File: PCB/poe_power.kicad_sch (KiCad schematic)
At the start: 44 parts, among them J1 Barrel_Jack, J7 Conn_01x02, Q1 MMBF170, U2 AP62200, U3 TPS2372, U6 MCP1792x-5002xCB, U7 VCB4805SBO-50WR3

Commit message: Started on board layout
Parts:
- removed J7: Conn_01x02, TerminalBlock_Phoenix:TerminalBlock_Phoenix_MKDS-1,5-2-5.08_1x02_P5.08mm_Horizontal, symbol Connector_Generic:Conn_01x02
- added J4: Screw_Terminal_01x02, TerminalBlock_Phoenix:TerminalBlock_Phoenix_MKDS-1,5-2-5.08_1x02_P5.08mm_Horizontal, symbol Connector:Screw_Terminal_01x02
- C19, C21: footprint (none) -> Capacitor_SMD:C_0805_2012Metric
- C20: footprint (none) -> Capacitor_SMD:C_Elec_6.3x5.8
- C23, C24, C25: footprint (none) -> Capacitor_SMD:C_Elec_6.3x5.4
- C6, C8: footprint Capacitor_SMD:C_0805_2012Metric_Pad1.18x1.45mm_HandSolder -> Capacitor_SMD:C_0805_2012Metric
- F1: footprint (none) -> Fuse:Fuse_1206_3216Metric
- L3: footprint (none) -> Inductor_SMD:L_0805_2012Metric
- R15, R16, R17, R18, R19, R20, R21, R22, R24, R25, R26, R29: footprint (none) -> Resistor_SMD:R_0805_2012Metric
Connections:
- net GND: now also J4.1 (Pin_1)
- net VIN: now also J4.2 (Pin_2)

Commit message: Started serious board layout
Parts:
- removed U2: AP62200, Package_TO_SOT_SMD:SOT-563, symbol Regulator_Switching:AP62250Z6
- added U2: AP62200WU-7, Package_TO_SOT_SMD:TSOT-23-6, symbol ProjectLibrary:AP62200WU-7
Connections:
- net GND: now also U2.1 (GND)
- net VIN: now also C7.1, C8.1
- net at R1.2, R4.1: now also U2.4 (FB)
- net at C1.1: now also U2.6 (BST)
- net at C1.2, L1.1: now also U2.2 (SW)
- net VLED: no longer names the net of C3.1, C4.1, L3.2
- net VLED: now also U2.3 (VIN), U2.5 (EN); no longer C7.1, C8.1

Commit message: Almost-Almost PCB design. Minor improvements on copper layer Silkscreen cleanup schematic sheet cleanup (now with subsheet titles)
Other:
- title: (none) -> Addressable LED Controller
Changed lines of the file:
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@@
 (kicad_sch (version 20230121) (generator eeschema)
   (paper "A4")
+  (title_block
+    (title "Addressable LED Controller")
+    (date "2023-07-30")
+    (rev "3.0")
+    (comment 1 "Jamal Bouajjaj")
+    (comment 2 "POE")
+  )
   (junction (at 138.43 146.05) (diameter 0) (color 0 0 0 0)
   )

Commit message: Final Rev 3 board
Many changes that are finalization changes mostly
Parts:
- removed Q1: MMBF170, Package_TO_SOT_SMD:SOT-23, symbol Transistor_FET:MMBF170
- added JP2: Jumper_2_Bridged, Connector_PinHeader_2.54mm:PinHeader_1x02_P2.54mm_Vertical, symbol Jumper:Jumper_2_Bridged
- U3: footprint Package_DFN_QFN:Texas_S-PVQFN-N20_EP3.15x3.15mm -> ProjectFootprints:TI_RGW0020B
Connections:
- net at R15.2, R22.1: now also JP2.2 (B)
- net at C19.2, D2.2 (-), D3.2 (-)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: now also JP2.1 (A)
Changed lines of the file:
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@@
-    (stroke (width 0) (type default))
-  )
-  (wire (pts (xy 106.68 53.34) (xy 106.68 50.8))
     (stroke (width 0) (type default))
   )
@@
     (stroke (width 0) (type default))
   )
-  (wire (pts (xy 88.9 77.47) (xy 113.03 77.47))
-    (stroke (width 0) (type default))
-  )
   (wire (pts (xy 106.68 146.05) (xy 111.76 146.05))
     (stroke (width 0) (type default))
@@
     (stroke (width 0) (type default))
   )
+  (wire (pts (xy 88.9 77.47) (xy 113.03 77.47))
+    (stroke (width 0) (type default))
+  )
   (wire (pts (xy 233.68 60.96) (xy 233.68 63.5))
+    (stroke (width 0) (type default))
+  )
+  (wire (pts (xy 106.68 50.8) (xy 106.68 53.34))
     (stroke (width 0) (type default))
   )
@@
     (effects (font (size 1.27 1.27)) (justify right))
   )
-  (hierarchical_label "POE_DIS" (shape input) (at 99.06 58.42 180) (fields_autoplaced)
-    (effects (font (size 1.27 1.27)) (justify right))
-  )
   (hierarchical_label "ETH_V2-" (shape input) (at 40.64 67.31 180) (fields_autoplaced)
     (effects (font (size 1.27 1.27)) (justify right))
@@
   (hierarchical_label "ETH_V1+" (shape input) (at 40.64 26.67 180) (fields_autoplaced)
     (effects (font (size 1.27 1.27)) (justify right))
+  )
+  (netclass_flag "" (length 2.54) (shape round) (at 82.55 43.18 0) (fields_autoplaced)
+    (effects (font (size 1.27 1.27)) (justify left bottom))
+    (property "Netclass" "HI_V" (at 83.439 40.64 0)
+      (effects (font (size 1.27 1.27) italic) (justify left))
+    )
+  )
+  (netclass_flag "" (length 2.54) (shape round) (at 73.66 50.8 0) (fields_autoplaced)
+    (effects (font (size 1.27 1.27)) (justify left bottom))
+    (property "Netclass" "HI_V" (at 74.549 48.26 0)
+      (effects (font (size 1.27 1.27) italic) (justify left))
+    )
   )
   (symbol (lib_id "Device:R") (at 121.92 48.26 90) (unit 1)
@@
         (path "/c2ef8e0f-ce81-4c82-a0ca-f054c5c3745d/1b44e26a-d4f8-4fcd-b6ed-54ad79d16191"
           (reference "D1") (unit 1)
-        )
-      )
-    )
-  )
-  (symbol (lib_id "Transistor_FET:MMBF170") (at 104.14 58.42 0) (unit 1)
-    (in_bom yes) (on_board yes) (dnp no)
-    (property "Reference" "Q1" (at 106.68 54.61 0)
-      (effects (font (size 1.27 1.27)) (justify left))
-    )
-    (property "Value" "MMBF170" (at 95.25 54.61 0)
-      (effects (font (size 1.27 1.27)) (justify left))
-    )
-    (property "Footprint" "Package_TO_SOT_SMD:SOT-23" (at 109.22 60.325 0)
-      (effects (font (size 1.27 1.27) italic) (justify left) hide)
-    )
-    (property "Datasheet" "https://www.diodes.com/assets/Datasheets/ds30104.pdf" (at 104.14 58.42 0)
-      (effects (font (size 1.27 1.27)) (justify left) hide)
-    )
-    (pin "1")
-    (pin "2")
-    (pin "3")
-    (instances
-      (project "LED_Controller"
-        (path "/c2ef8e0f-ce81-4c82-a0ca-f054c5c3745d"
-          (reference "Q1") (unit 1)
-        )
-        (path "/c2ef8e0f-ce81-4c82-a0ca-f054c5c3745d/1b44e26a-d4f8-4fcd-b6ed-54ad79d16191"
-          (reference "Q1") (unit 1)
         )
       )
@@
     )
   )
+  (symbol (lib_id "Jumper:Jumper_2_Bridged") (at 106.68 58.42 90) (unit 1)
+    (in_bom yes) (on_board yes) (dnp no) (fields_autoplaced)
+    (property "Reference" "JP2" (at 107.95 57.15 90)
+      (effects (font (size 1.27 1.27)) (justify right))
+    )
+    (property "Value" "Jumper_2_Bridged" (at 107.95 59.69 90)
+      (effects (font (size 1.27 1.27)) (justify right) hide)
+    )
+    (property "Footprint" "Connector_PinHeader_2.54mm:PinHeader_1x02_P2.54mm_Vertical" (at 106.68 58.42 0)
+      (effects (font (size 1.27 1.27)) hide)
+    )
+    (property "Datasheet" "~" (at 106.68 58.42 0)
+      (effects (font (size 1.27 1.27)) hide)
+    )
+    (pin "1")
+    (pin "2")
+    (instances
+      (project "LED_Controller"
+        (path "/c2ef8e0f-ce81-4c82-a0ca-f054c5c3745d/1b44e26a-d4f8-4fcd-b6ed-54ad79d16191"
+          (reference "JP2") (unit 1)
+        )
+      )
+    )
+  )
   (symbol (lib_id "Device:Polyfuse") (at 90.17 128.27 90) (unit 1)
     (in_bom yes) (on_board yes) (dnp no) (fields_autoplaced)
@@
       (effects (font (size 1.27 1.27)))
     )
-    (property "Footprint" "Package_DFN_QFN:Texas_S-PVQFN-N20_EP3.15x3.15mm" (at 140.97 55.88 0)
-      (effects (font (size 1.27 1.27)) hide)
-    )
+    (property "Footprint" "ProjectFootprints:TI_RGW0020B" (at 140.97 55.88 0)
+      (effects (font (size 1.27 1.27)) hide)
+    )

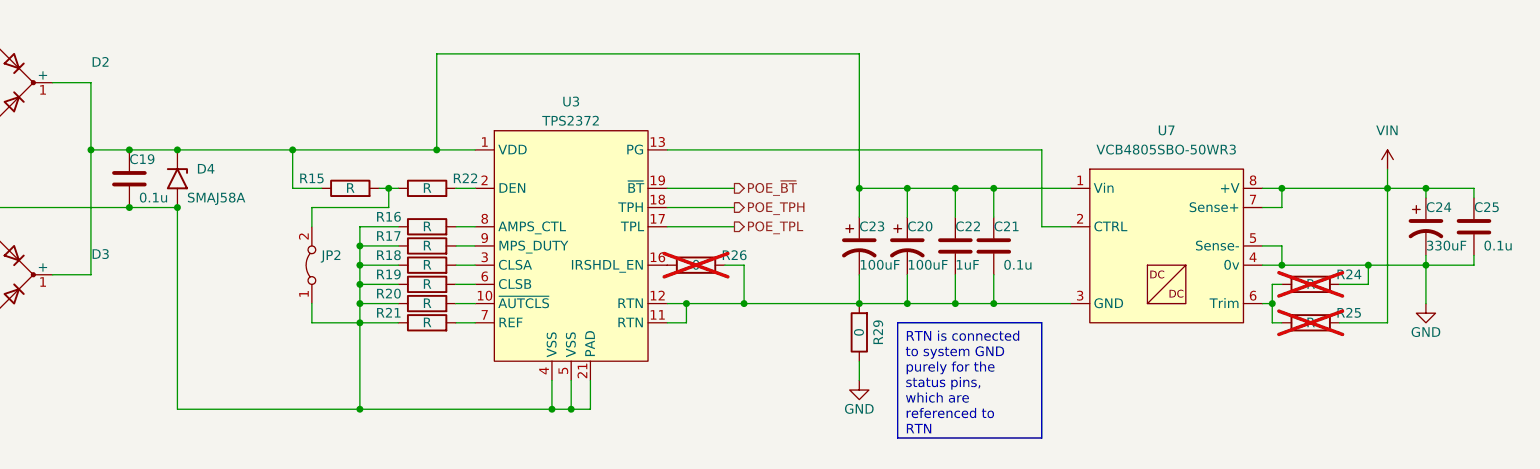
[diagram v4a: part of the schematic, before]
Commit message: Updated schematic on repo. Added so cap have voltage rating on schematic
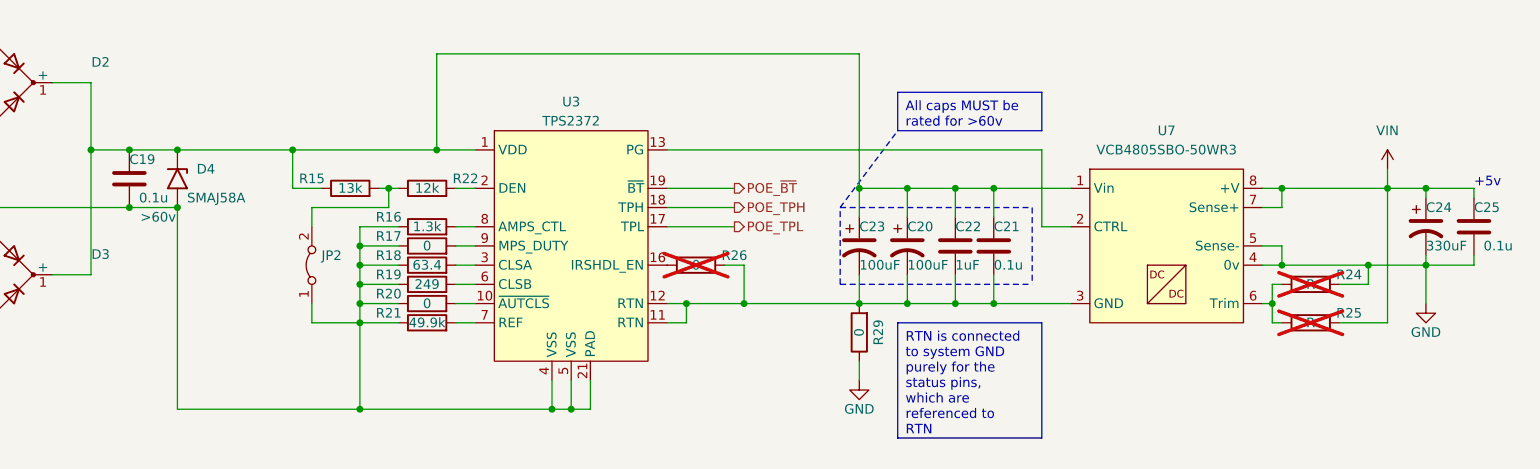
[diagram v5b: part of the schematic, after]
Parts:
- C19: Voltage (none) -> >60v
- R15: value R -> 13k
- R16: value R -> 1.3k
- R17, R20: value R -> 0
- R18: value R -> 63.4
- R19: value R -> 249
- R21: value R -> 49.9k
- R22: value R -> 12k
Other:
- note added: "+5v"
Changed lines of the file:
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@@
     (stroke (width 0) (type default))
+  )
+  (polyline (pts (xy 176.53 60.96) (xy 176.53 50.8))
+    (stroke (width 0) (type dash))
   )
   (wire (pts (xy 148.59 128.27) (xy 149.86 128.27))
@@
     (stroke (width 0) (type solid))
   )
+  (polyline (pts (xy 176.53 60.96) (xy 201.93 60.96))
+    (stroke (width 0) (type dash))
+  )
   (wire (pts (xy 162.56 143.51) (xy 162.56 146.05))
     (stroke (width 0) (type default))
@@
     (stroke (width 0) (type default))
   )
+  (polyline (pts (xy 201.93 50.8) (xy 201.93 60.96))
+    (stroke (width 0) (type dash))
+  )
   (wire (pts (xy 191.77 63.5) (xy 196.85 63.5))
     (stroke (width 0) (type default))
@@
     (stroke (width 0) (type default))
   )
+  (polyline (pts (xy 176.53 50.8) (xy 201.93 50.8))
+    (stroke (width 0) (type dash))
+  )
   (wire (pts (xy 181.61 143.51) (xy 181.61 144.78))
     (stroke (width 0) (type solid))
@@
     (stroke (width 0) (type default))
   )
+  (polyline (pts (xy 176.53 50.8) (xy 184.15 40.64))
+    (stroke (width 0) (type dash))
+  )
   (wire (pts (xy 196.85 59.69) (xy 196.85 63.5))
     (stroke (width 0) (type default))
@@
     (fill (type none))
     (effects (font (size 1.27 1.27)) (justify left top))
+  )
+  (text_box "All caps MUST be rated for >60v"
+    (at 184.15 35.56 0) (size 19.05 5.08)
+    (stroke (width 0) (type default))
+    (fill (type none))
+    (effects (font (size 1.27 1.27)) (justify left top))
+  )
+  (text "+5v" (at 260.35 48.26 0)
+    (effects (font (size 1.27 1.27)) (justify left bottom))
   )
   (hierarchical_label "POE_~{BT}" (shape output) (at 162.56 48.26 0) (fields_autoplaced)
@@
       (effects (font (size 1.27 1.27)))
     )
-    (property "Value" "R" (at 121.92 48.26 90)
+    (property "Value" "12k" (at 121.92 48.26 90)
       (effects (font (size 1.27 1.27)))
     )
@@
       (effects (font (size 1.27 1.27)))
     )
-    (property "Value" "R" (at 121.92 53.34 90)
+    (property "Value" "1.3k" (at 121.92 53.34 90)
       (effects (font (size 1.27 1.27)))
     )
@@
       (effects (font (size 1.27 1.27)))
     )
-    (property "Value" "R" (at 121.92 60.96 90)
+    (property "Value" "249" (at 121.92 60.96 90)
       (effects (font (size 1.27 1.27)))
     )
@@
       (effects (font (size 1.27 1.27)))
     )
-    (property "Value" "R" (at 121.92 55.88 90)
+    (property "Value" "0" (at 121.92 55.88 90)
       (effects (font (size 1.27 1.27)))
     )
@@
       (effects (font (size 1.27 1.27)) hide)
     )
+    (property "Voltage" ">60v" (at 86.36 52.07 0)
+      (effects (font (size 1.27 1.27)))
+    )
     (pin "1")
     (pin "2")
@@
       (effects (font (size 1.27 1.27)))
     )
-    (property "Value" "R" (at 121.92 63.5 90)
+    (property "Value" "0" (at 121.92 63.5 90)
       (effects (font (size 1.27 1.27)))
     )
@@
       (effects (font (size 1.27 1.27)))
     )
-    (property "Value" "R" (at 121.92 58.42 90)
+    (property "Value" "63.4" (at 121.92 58.42 90)
       (effects (font (size 1.27 1.27)))
     )
@@
       (effects (font (size 1.27 1.27)))
     )
-    (property "Value" "R" (at 121.92 66.04 90)
+    (property "Value" "49.9k" (at 121.92 66.04 90)
       (effects (font (size 1.27 1.27)))
     )
@@
       (effects (font (size 1.27 1.27)))
     )
-    (property "Value" "R" (at 111.76 48.26 90)
+    (property "Value" "13k" (at 111.76 48.26 90)
       (effects (font (size 1.27 1.27)))
     )
@@
       (effects (font (size 1.27 1.27)) (justify left))
     )
-    (property "Value" "0.1u" (at 198.12 58.42 0)
-      (effects (font (size 1.27 1.27)) (justify left))
-    )
+    (property "Value" "0.1u" (at 196.85 58.42 0)
+      (effects (font (size 1.27 1.27)) (justify left))
+    )
